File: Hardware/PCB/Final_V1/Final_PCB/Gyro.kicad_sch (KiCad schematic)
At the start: 9 parts, among them U1 MPU-6050

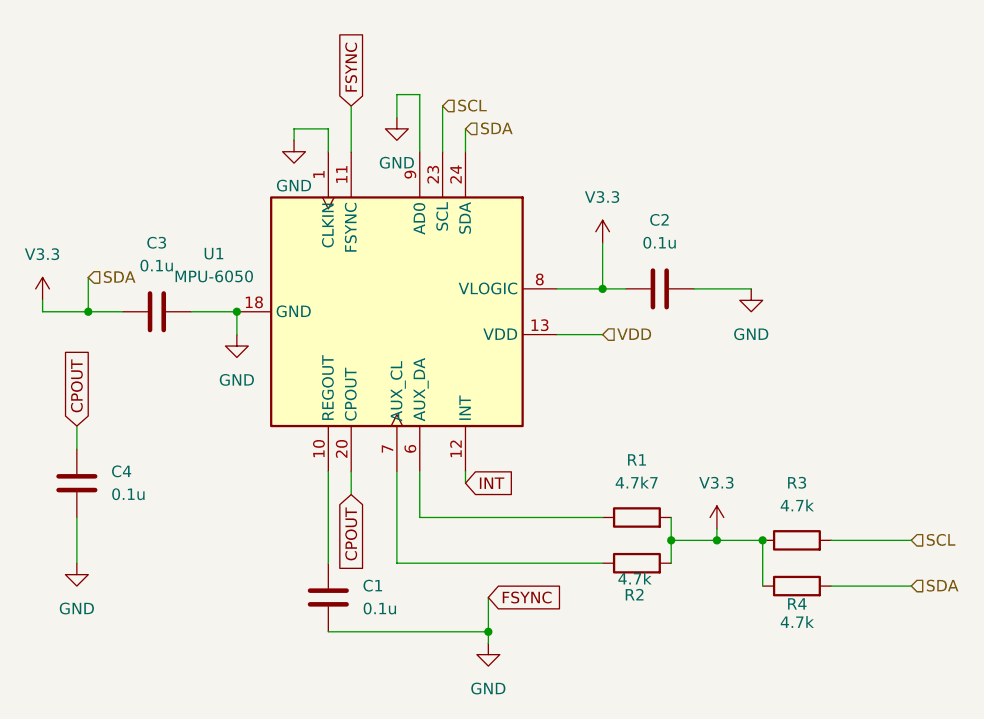
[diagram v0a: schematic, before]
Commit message: added Voltage regulator to get constant 3.3V Voltage and fixed some issues
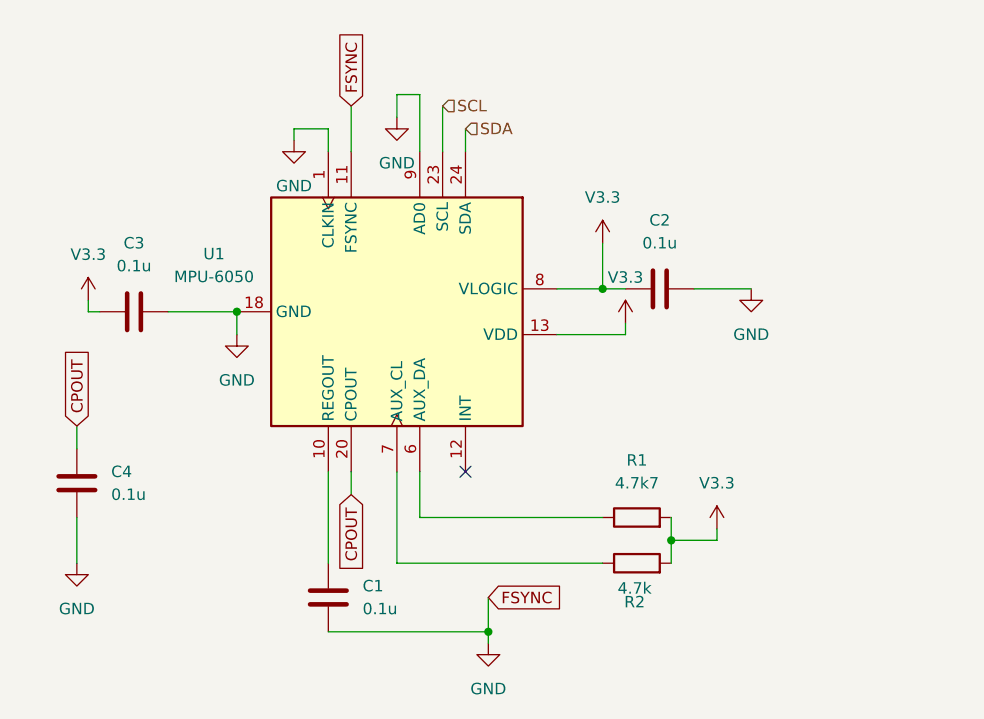
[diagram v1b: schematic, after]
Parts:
- removed R3, R4: 4.7k, Resistor_SMD:R_0603_1608Metric, symbol Device:R
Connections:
- net VDD is gone; now on net V3.3: U1.13 (VDD)
- net V3.3: no longer U1.24 (SDA)
- net INT: no longer names the net of U1.12 (INT)
- new net SDA: U1.24 (SDA)
- no-connect marks 0 -> 1
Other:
- moved on the sheet: C3

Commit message: fixing xhematics
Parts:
- renumbered C2 to C12, C1 to C14, U1 to U11
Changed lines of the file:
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@@
 		(dnp no)
 		(fields_autoplaced yes)
-		(property "Reference" "C1"
+		(property "Reference" "C14"
 			(at 125.73 111.7599 0)
 			(effects
@@
 			(project "Final_PCB"
 				(path "/3cedac76-cdf6-4427-9720-a412bd9af7e2/a2088990-a8d7-4850-b98e-ebf370362bc3"
-					(reference "C1")
+					(reference "C14")
 					(unit 1)
 				)
@@
 		(dnp no)
 		(fields_autoplaced yes)
-		(property "Reference" "C2"
+		(property "Reference" "C12"
 			(at 158.75 71.12 90)
 			(effects
@@
 			(project "Final_PCB"
 				(path "/3cedac76-cdf6-4427-9720-a412bd9af7e2/a2088990-a8d7-4850-b98e-ebf370362bc3"
-					(reference "C2")
+					(reference "C12")
 					(unit 1)
 				)
@@
 		(dnp no)
 		(fields_autoplaced yes)
-		(property "Reference" "U1"
+		(property "Reference" "U11"
 			(at 109.22 74.8598 90)
 			(effects
@@
 			(project "Final_PCB"
 				(path "/3cedac76-cdf6-4427-9720-a412bd9af7e2/a2088990-a8d7-4850-b98e-ebf370362bc3"
-					(reference "U1")
-					(unit 1)
-				)
+					(reference "U11")
+					(unit 1)
+				)

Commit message: #1: Add footprints to the components
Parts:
- U11: footprint Sensor_Motion:InvenSense_QFN-24_4x4mm_P0.5mm -> (none)
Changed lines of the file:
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@@
 			)
 		)
-		(property "Footprint" "Sensor_Motion:InvenSense_QFN-24_4x4mm_P0.5mm"
+		(property "Footprint" ""
 			(at 109.22 81.28 0)
 			(effects

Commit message: #3: fix-1-footprint
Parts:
- U11: footprint (none) -> Sensor_Motion:InvenSense_QFN-24_4x4mm_P0.5mm
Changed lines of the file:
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@@
 			)
 		)
-		(property "Footprint" ""
+		(property "Footprint" "Sensor_Motion:InvenSense_QFN-24_4x4mm_P0.5mm"
 			(at 109.22 81.28 0)
 			(effects
